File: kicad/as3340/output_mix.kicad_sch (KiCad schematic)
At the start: 29 parts, among them U1 TL074, U16 LM4040CIM3-2.5, U5 MAX333A, U6 AS3360, U8 DG442CY+

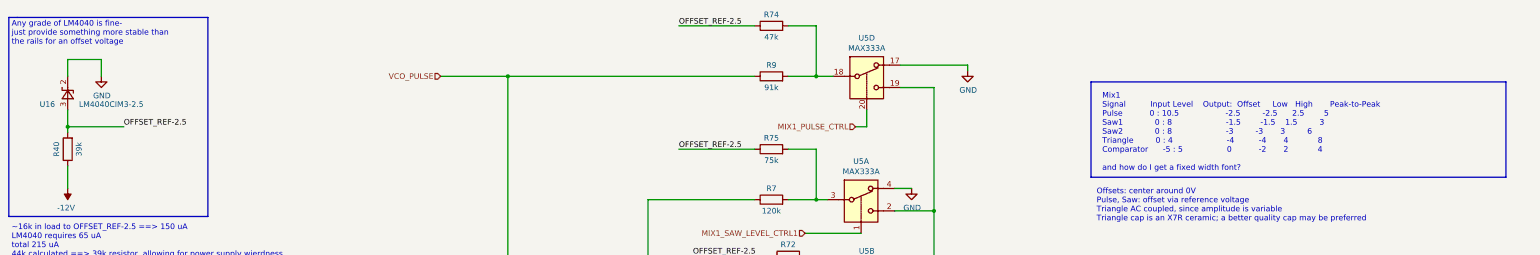
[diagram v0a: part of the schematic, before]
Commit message: starting updates for v0.5
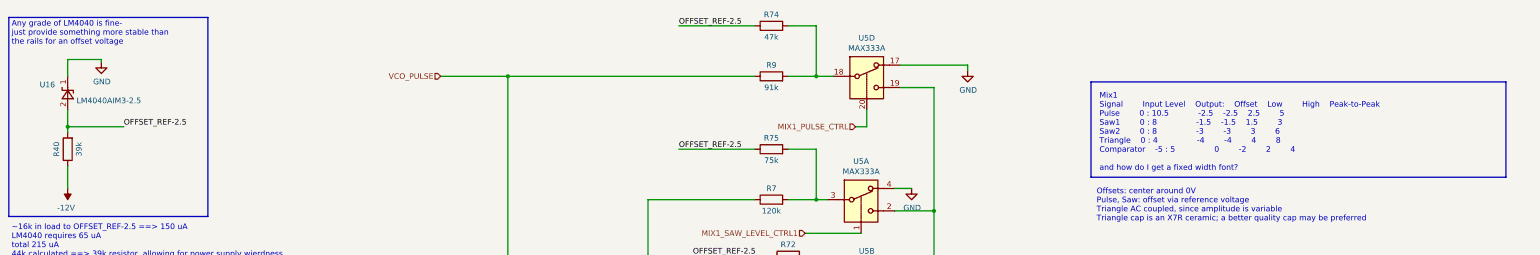
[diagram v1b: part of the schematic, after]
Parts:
- removed U16: LM4040CIM3-2.5, Package_TO_SOT_SMD:SOT-23, symbol Reference_Voltage:LM4040LP-4.1
- added U16: LM4040AIM3-2.5, Package_TO_SOT_SMD:SOT-23, symbol Reference_Voltage:LM4040DBZ-2.5
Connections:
- net GND: now also U16.1 (K)
- net OFFSET_REF-2.5: now also U16.2 (A)
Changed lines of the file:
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@@
     (stroke (width 0) (type default) (color 0 0 0 0))
   )
-  (wire (pts (xy 78.105 25.4) (xy 78.105 29.21))
+  (wire (pts (xy 78.105 25.4) (xy 78.105 26.035))
     (stroke (width 0) (type default) (color 0 0 0 0))
   )
@@
     (stroke (width 0) (type default) (color 0 0 0 0))
   )
-  (text "Mix1\nSignal          Input Level    Output:  Offset     Low   High       Peak-to-Peak\nPulse           0 : 10.5                   -2.5         -2.5      2.5        5\nSaw1             0 : 8                      -1.5        -1.5    1.5         3\nSaw2             0 : 8                      -3         -3       3         6\nTriangle         0 : 4                      -4          -4       4            8\nComparator      -5 : 5                  0           -2       2            4\n\nand how do I get a fixed width font?"
-    (at 304.8 50.8 0)
+  (text "Mix1\nSignal		Input Level	Output:	Offset	Low		High	Peak-to-Peak\nPulse		0 : 10.5			-2.5	-2.5	2.5		5\nSaw1		0 : 8				-1.5	-1.5	1.5		3\nSaw2		0 : 8				-3		-3		3		6\nTriangle	0 : 4				-4		-4		4		8\nComparator	-5 : 5				0		-2		2		4\n\nand how do I get a fixed width font?"
+    (at 304.165 50.8 0)
     (effects (font (size 1.27 1.27)) (justify left bottom))
   )
@@
     (pin "1")
   )
+  (symbol (lib_id "Reference_Voltage:LM4040DBZ-2.5") (at 70.485 33.02 90) (unit 1)
+    (in_bom yes) (on_board yes)
+    (property "Reference" "U16" (id 0) (at 64.135 31.115 90)
+      (effects (font (size 1.27 1.27)) (justify right))
+    )
+    (property "Value" "LM4040AIM3-2.5" (id 1) (at 72.4916 34.7222 90)
+      (effects (font (size 1.27 1.27)) (justify right))
+    )
+    (property "Footprint" "Package_TO_SOT_SMD:SOT-23" (id 2) (at 75.565 33.02 0)
+      (effects (font (size 1.27 1.27) italic) hide)
+    )
+    (property "Datasheet" "http://www.ti.com/lit/ds/symlink/lm4040-n.pdf" (id 3) (at 70.485 33.02 0)
+      (effects (font (size 1.27 1.27) italic) hide)
+    )
+    (property "LCSC Part" "C131939" (id 4) (at 70.485 33.02 90)
+      (effects (font (size 1.27 1.27)) hide)
+    )
+    (pin "1")
+    (pin "2")
+  )
   (symbol (lib_id "Device:C") (at 257.81 116.84 270) (unit 1)
     (in_bom yes) (on_board yes)
@@
     (pin "1")
   )
-  (symbol (lib_id "power:GND") (at 78.105 29.21 0) (unit 1)
-    (in_bom yes) (on_board yes)
-    (property "Reference" "#PWR042" (id 0) (at 78.105 35.56 0)
-      (effects (font (size 1.27 1.27)) hide)
-    )
-    (property "Value" "GND" (id 1) (at 78.232 33.6042 0))
-    (property "Footprint" "" (id 2) (at 78.105 29.21 0)
-      (effects (font (size 1.27 1.27)) hide)
-    )
-    (property "Datasheet" "" (id 3) (at 78.105 29.21 0)
+  (symbol (lib_id "power:GND") (at 78.105 26.035 0) (unit 1)
+    (in_bom yes) (on_board yes)
+    (property "Reference" "#PWR042" (id 0) (at 78.105 32.385 0)
+      (effects (font (size 1.27 1.27)) hide)
+    )
+    (property "Value" "GND" (id 1) (at 78.232 30.4292 0))
+    (property "Footprint" "" (id 2) (at 78.105 26.035 0)
+      (effects (font (size 1.27 1.27)) hide)
+    )
+    (property "Datasheet" "" (id 3) (at 78.105 26.035 0)
       (effects (font (size 1.27 1.27)) hide)
     )
@@
     (pin "1")
   )
-  (symbol (lib_id "Reference_Voltage:LM4040LP-4.1") (at 70.485 33.02 90) (unit 1)
-    (in_bom yes) (on_board yes)
-    (property "Reference" "U16" (id 0) (at 64.135 35.56 90)
-      (effects (font (size 1.27 1.27)) (justify right))
-    )
-    (property "Value" "LM4040CIM3-2.5" (id 1) (at 73.025 35.56 90)
-      (effects (font (size 1.27 1.27)) (justify right))
-    )
-    (property "Footprint" "Package_TO_SOT_SMD:SOT-23" (id 2) (at 75.565 33.02 0)
-      (effects (font (size 1.27 1.27) italic) hide)
-    )
-    (property "Datasheet" "http://www.ti.com/lit/ds/symlink/lm4040-n.pdf" (id 3) (at 70.485 33.02 0)
-      (effects (font (size 1.27 1.27) italic) hide)
-    )
-    (property "LCSC Part" "C131939" (id 5) (at 70.485 33.02 0)
-      (effects (font (size 1.27 1.27)) hide)
-    )
-    (property "Digikey" "LM4040BIZ-2.5/NOPB-ND" (id 6) (at 70.485 33.02 0)
-      (effects (font (size 1.27 1.27)) hide)
-    )
-    (pin "2")
-    (pin "3")
-  )
 )

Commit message: output levels
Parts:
- R6: value 62k -> 91k; LCSC Part C23221 -> C23265
- R7: value 120k -> 180k; LCSC Part C25808 -> C22827
- R72: value 39k -> 56k; LCSC Part C23153 -> C23206
- R74: value 47k -> 62k; LCSC Part C25819 -> C23221
- R75: value 75k -> 110k; LCSC Part C23242 -> C25805
- R9: value 91k -> 120k; LCSC Part C23265 -> C25808
- U5: footprint (none) -> Package_SO:SOIC-20W_7.5x12.8mm_P1.27mm
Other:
- note added: "Mix1 Signal Input Level Output: Offset Low High Peak-to-Peak Pulse 0 : 10.5 -1.9 -1.9 2.0 4.0 Saw1 0 : 8 -1.0 -1.0 1.0 2 Saw2 0 : 8 -2.1 -2.1 2.0 4.0 Triangle 0 : 3.5 AC -1.7 1.7 3.5 Comparator -5 : 5 0 -2 2 4 Mix2 Pulse 0 : 10.5 0.0 0.0 3.1 3.1 Saw1 0 : 8 0.0 0.0 3.8 3.8"
- note added: "Offsets: mix1 center roughly around 0V Pulse, Saw: offset via reference voltage Triangle AC coupled, since amplitude is variable Triangle cap is an X7R ceramic; a better quality cap may be preferred"
- note removed: "Mix1 Signal Input Level Output: Offset Low High Peak-to-Peak Pulse 0 : 10.5 -2.5 -2.5 2.5 5 Saw1 0 : 8 -1.5 -1.5 1.5 3 Saw2 0 : 8 -3 -3 3 6 Triangle 0 : 4 -4 -4 4 8 Comparator -5 : 5 0 -2 2 4 and how do I get a fixed width font?"
- note removed: "Offsets: center around 0V Pulse, Saw: offset via reference voltage Triangle AC coupled, since amplitude is variable Triangle cap is an X7R ceramic; a better quality cap may be preferred"
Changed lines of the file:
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@@
     (stroke (width 0) (type default) (color 0 0 0 0))
   )
-  (text "Mix1\nSignal		Input Level	Output:	Offset	Low		High	Peak-to-Peak\nPulse		0 : 10.5			-2.5	-2.5	2.5		5\nSaw1		0 : 8				-1.5	-1.5	1.5		3\nSaw2		0 : 8				-3		-3		3		6\nTriangle	0 : 4				-4		-4		4		8\nComparator	-5 : 5				0		-2		2		4\n\nand how do I get a fixed width font?"
+  (text "Mix1\nSignal		Input Level	Output:	Offset	Low		High	Peak-to-Peak\nPulse		0 : 10.5			-1.9	-1.9	2.0		4.0\nSaw1		0 : 8				-1.0	-1.0	1.0		2\nSaw2		0 : 8				-2.1	-2.1	2.0		4.0\nTriangle	0 : 3.5				AC		-1.7	1.7		3.5\nComparator	-5 : 5				0		-2		2		4\n\nMix2\nPulse		0 : 10.5			0.0		0.0		3.1		3.1\nSaw1		0 : 8				0.0		0.0		3.8		3.8"
     (at 304.165 50.8 0)
     (effects (font (size 1.27 1.27)) (justify left bottom))
   )
-  (text "Offsets: center around 0V\nPulse, Saw: offset via reference voltage\nTriangle AC coupled, since amplitude is variable\nTriangle cap is an X7R ceramic; a better quality cap may be preferred\n"
+  (text "Offsets: mix1 center roughly around 0V\nPulse, Saw: offset via reference voltage\nTriangle AC coupled, since amplitude is variable\nTriangle cap is an X7R ceramic; a better quality cap may be preferred\n"
     (at 303.53 62.23 0)
     (effects (font (size 1.27 1.27)) (justify left bottom))
@@
     (in_bom yes) (on_board yes)
     (property "Reference" "R9" (id 0) (at 229.87 26.67 90))
-    (property "Value" "91k" (id 1) (at 229.87 31.75 90))
+    (property "Value" "120k" (id 1) (at 229.87 31.75 90))
     (property "Footprint" "Resistor_SMD:R_0603_1608Metric" (id 2) (at 229.87 30.988 90)
       (effects (font (size 1.27 1.27)) hide)
@@
       (effects (font (size 1.27 1.27)) hide)
     )
-    (property "LCSC Part" "C23265" (id 4) (at 229.87 29.21 0)
+    (property "LCSC Part" "C25808" (id 4) (at 229.87 29.21 0)
       (effects (font (size 1.27 1.27)) hide)
     )
@@
     (in_bom yes) (on_board yes)
     (property "Reference" "R6" (id 0) (at 218.44 74.93 90))
-    (property "Value" "62k" (id 1) (at 218.44 80.01 90))
+    (property "Value" "91k" (id 1) (at 218.44 80.01 90))
     (property "Footprint" "Resistor_SMD:R_0603_1608Metric" (id 2) (at 218.44 79.248 90)
       (effects (font (size 1.27 1.27)) hide)
@@
       (effects (font (size 1.27 1.27)) hide)
     )
-    (property "LCSC Part" "C23221" (id 4) (at 218.44 77.47 0)
+    (property "LCSC Part" "C23265" (id 4) (at 218.44 77.47 0)
       (effects (font (size 1.27 1.27)) hide)
     )
@@
     (in_bom yes) (on_board yes)
     (property "Reference" "R7" (id 0) (at 229.87 54.61 90))
-    (property "Value" "120k" (id 1) (at 229.87 59.69 90))
+    (property "Value" "180k" (id 1) (at 229.87 59.69 90))
     (property "Footprint" "Resistor_SMD:R_0603_1608Metric" (id 2) (at 229.87 58.928 90)
       (effects (font (size 1.27 1.27)) hide)
@@
       (effects (font (size 1.27 1.27)) hide)
     )
-    (property "LCSC Part" "C25808" (id 4) (at 229.87 57.15 0)
+    (property "LCSC Part" "C22827" (id 4) (at 229.87 57.15 0)
       (effects (font (size 1.27 1.27)) hide)
     )
@@
     (property "Reference" "U5" (id 0) (at 251.46 20.5232 0))
     (property "Value" "MAX333A" (id 1) (at 251.46 22.8346 0))
-    (property "Footprint" "" (id 2) (at 251.46 26.67 0)
+    (property "Footprint" "Package_SO:SOIC-20W_7.5x12.8mm_P1.27mm" (id 2) (at 251.46 26.67 0)
       (effects (font (size 1.27 1.27)) hide)
     )
@@
     (in_bom yes) (on_board yes)
     (property "Reference" "R74" (id 0) (at 229.87 15.24 90))
-    (property "Value" "47k" (id 1) (at 229.87 20.32 90))
+    (property "Value" "62k" (id 1) (at 229.87 20.32 90))
     (property "Footprint" "Resistor_SMD:R_0603_1608Metric" (id 2) (at 229.87 19.558 90)
       (effects (font (size 1.27 1.27)) hide)
@@
       (effects (font (size 1.27 1.27)) hide)
     )
-    (property "LCSC Part" "C25819" (id 4) (at 229.87 17.78 0)
+    (property "LCSC Part" "C23221" (id 4) (at 229.87 17.78 0)
       (effects (font (size 1.27 1.27)) hide)
     )
@@
     (property "Reference" "U5" (id 0) (at 250.19 48.4632 0))
     (property "Value" "MAX333A" (id 1) (at 250.19 50.7746 0))
-    (property "Footprint" "" (id 2) (at 250.19 54.61 0)
+    (property "Footprint" "Package_SO:SOIC-20W_7.5x12.8mm_P1.27mm" (id 2) (at 250.19 54.61 0)
       (effects (font (size 1.27 1.27)) hide)
     )
@@
     (in_bom yes) (on_board yes)
     (property "Reference" "R75" (id 0) (at 229.87 43.18 90))
-    (property "Value" "75k" (id 1) (at 229.87 48.26 90))
+    (property "Value" "110k" (id 1) (at 229.87 48.26 90))
     (property "Footprint" "Resistor_SMD:R_0603_1608Metric" (id 2) (at 229.87 47.498 90)
       (effects (font (size 1.27 1.27)) hide)
@@
       (effects (font (size 1.27 1.27)) hide)
     )
-    (property "LCSC Part" "C23242" (id 4) (at 229.87 45.72 0)
+    (property "LCSC Part" "C25805" (id 4) (at 229.87 45.72 0)
       (effects (font (size 1.27 1.27)) hide)
     )
@@
     (property "Reference" "U5" (id 0) (at 251.46 68.7832 0))
     (property "Value" "MAX333A" (id 1) (at 251.46 71.0946 0))
-    (property "Footprint" "" (id 2) (at 251.46 74.93 0)
+    (property "Footprint" "Package_SO:SOIC-20W_7.5x12.8mm_P1.27mm" (id 2) (at 251.46 74.93 0)
       (effects (font (size 1.27 1.27)) hide)
     )
@@
     (in_bom yes) (on_board yes)
     (property "Reference" "R72" (id 0) (at 233.68 67.31 90))
-    (property "Value" "39k" (id 1) (at 233.68 72.39 90))
+    (property "Value" "56k" (id 1) (at 233.68 72.39 90))
     (property "Footprint" "Resistor_SMD:R_0603_1608Metric" (id 2) (at 233.68 71.628 90)
       (effects (font (size 1.27 1.27)) hide)
@@
       (effects (font (size 1.27 1.27)) hide)
     )
-    (property "LCSC Part" "C23153" (id 4) (at 233.68 69.85 0)
+    (property "LCSC Part" "C23206" (id 4) (at 233.68 69.85 0)
       (effects (font (size 1.27 1.27)) hide)
     )
@@
     (property "Reference" "U5" (id 0) (at 250.19 89.1032 0))
     (property "Value" "MAX333A" (id 1) (at 250.19 91.4146 0))
-    (property "Footprint" "" (id 2) (at 250.19 95.25 0)
-      (effects (font (size 1.27 1.27)) hide)
-    )
+    (property "Footprint" "Package_SO:SOIC-20W_7.5x12.8mm_P1.27mm" (id 2) (at 250.19 95.25 0)
+      (effects (font (size 1.27 1.27)) hide)
+    )

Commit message: gerbers and build artifacts produced
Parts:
- U16: LCSC Part C131939 -> C460725
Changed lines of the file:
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@@
       (effects (font (size 1.27 1.27) italic) hide)
     )
-    (property "LCSC Part" "C131939" (id 4) (at 70.485 33.02 90)
+    (property "LCSC Part" "C460725" (id 4) (at 70.485 33.02 90)
       (effects (font (size 1.27 1.27)) hide)
     )

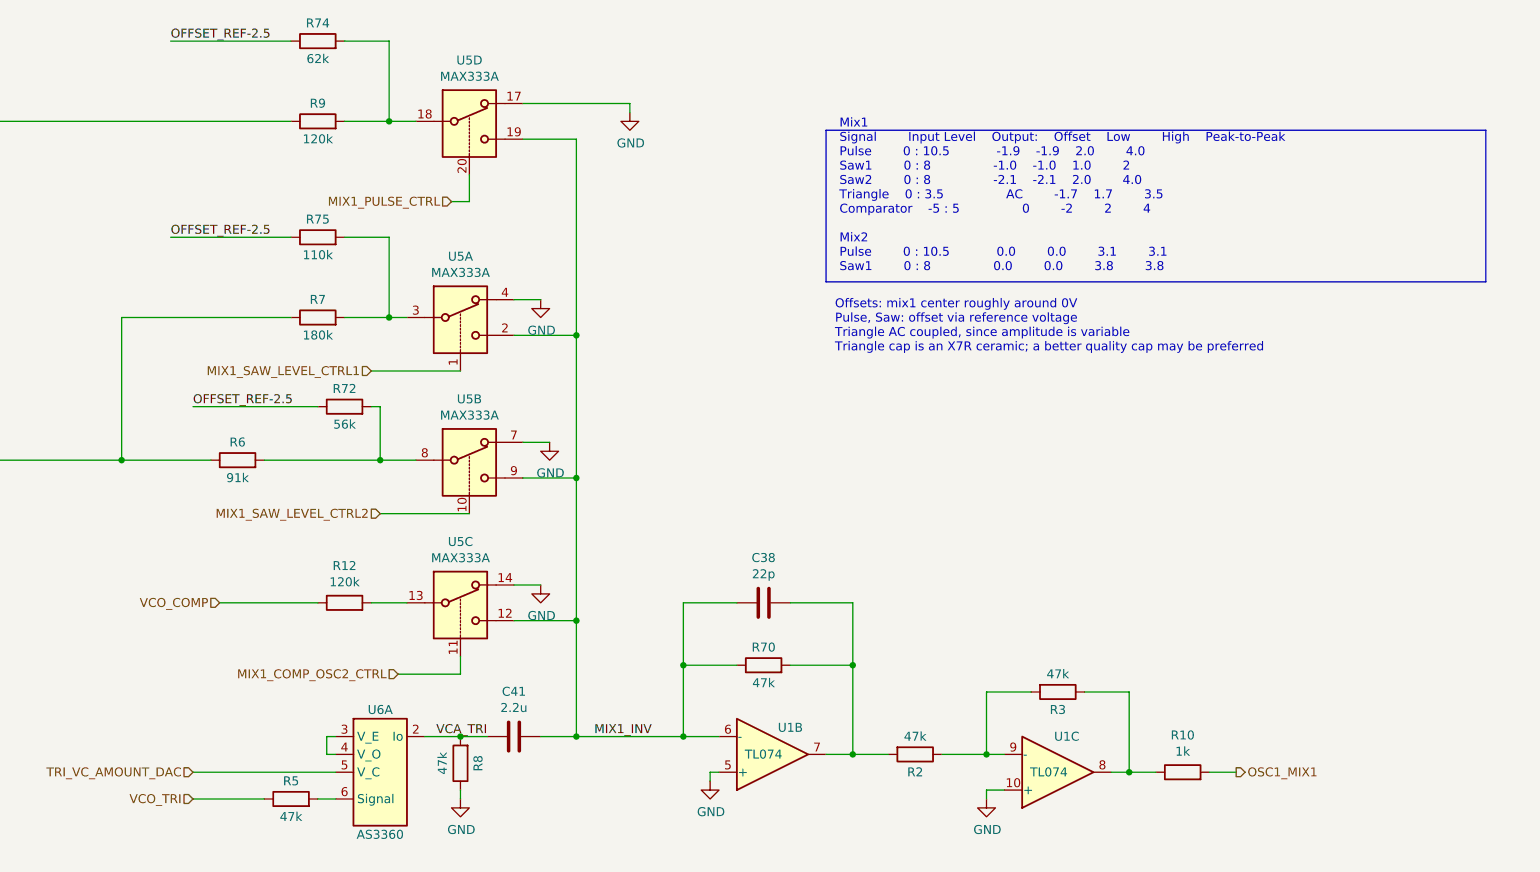
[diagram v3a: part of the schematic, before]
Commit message: output levels changed and other fixes
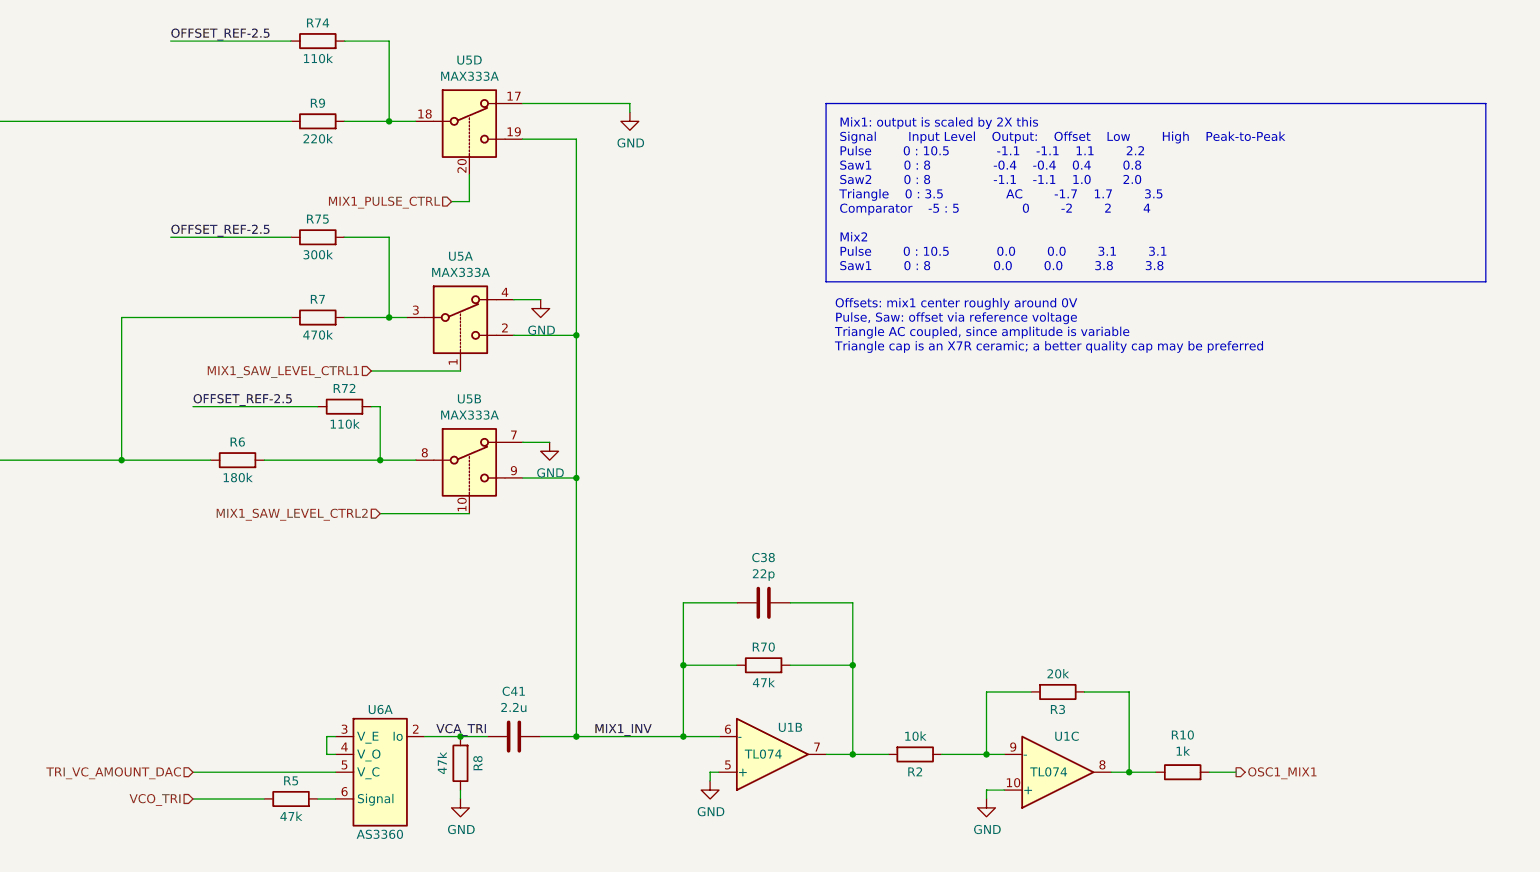
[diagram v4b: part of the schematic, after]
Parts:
- removed R12: 120k, Resistor_SMD:R_0603_1608Metric, symbol Device:R
- removed unit 3 of U5
- R2: value 47k -> 10k; LCSC Part C25819 -> (none)
- R3: value 47k -> 20k; LCSC Part C25819 -> (none)
- R6: value 91k -> 180k; LCSC Part C23265 -> (none)
- R7: value 180k -> 470k; LCSC Part C22827 -> (none)
- R72: value 56k -> 110k; LCSC Part C23206 -> (none)
- R74: value 62k -> 110k; LCSC Part C23221 -> (none)
- R75: value 110k -> 300k
- R9: value 120k -> 220k; LCSC Part C25808 -> (none)
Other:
- note added: "Mix1: output is scaled by 2X this Signal Input Level Output: Offset Low High Peak-to-Peak Pulse 0 : 10.5 -1.1 -1.1 1.1 2.2 Saw1 0 : 8 -0.4 -0.4 0.4 0.8 Saw2 0 : 8 -1.1 -1.1 1.0 2.0 Triangle 0 : 3.5 AC -1.7 1.7 3.5 Comparator -5 : 5 0 -2 2 4 Mix2 Pulse 0 : 10.5 0.0 0.0 3.1 3.1 Saw1 0 : 8 0.0 0.0 3.8 3.8"
- note removed: "Mix1 Signal Input Level Output: Offset Low High Peak-to-Peak Pulse 0 : 10.5 -1.9 -1.9 2.0 4.0 Saw1 0 : 8 -1.0 -1.0 1.0 2 Saw2 0 : 8 -2.1 -2.1 2.0 4.0 Triangle 0 : 3.5 AC -1.7 1.7 3.5 Comparator -5 : 5 0 -2 2 4 Mix2 Pulse 0 : 10.5 0.0 0.0 3.1 3.1 Saw1 0 : 8 0.0 0.0 3.8 3.8"

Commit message: changed output scaling; CV freq range; removed comp output
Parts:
- R2: LCSC Part (none) -> C25804
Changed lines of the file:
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@@
       (effects (font (size 1.27 1.27)) hide)
     )
-    (property "LCSC Part" "" (id 4) (at 314.96 119.38 0)
+    (property "LCSC Part" "C25804" (id 4) (at 314.96 119.38 0)
       (effects (font (size 1.27 1.27)) hide)
     )
